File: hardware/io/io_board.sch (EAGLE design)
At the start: 64 parts, among them IC4 74HCT139N, IC5 74AC06N, IC6 8251A, IC7 MAX232, J1 DIN5, T1 BC847, X2 CRYSTALS-NOGND-CFPX-217

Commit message: PCB project fixed
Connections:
- net IO_RD: now also IC3.RD
- net IO_WR: now also IC3.WR
- net RD: no longer IC3.RD
- net WR: no longer IC3.WR

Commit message: Buffer added to D0..D7 lined of CF card
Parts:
- added C26: 100N, rcl:C-EUC0603
- added IC11: 74HCT245DW, 74xx-eu:74HCT245DW
- R5: device rcl:R-EU_R0603 -> rcl:R-EU_0207/10
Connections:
- new net CF_D0: CON1G$1.D00, IC11A.B8
- new net CF_D1: CON1G$1.D01, IC11A.B7
- new net CF_D2: CON1G$1.D02, IC11A.B6
- new net CF_D3: CON1G$1.D03, IC11A.B1
- new net CF_D4: CON1G$1.D04, IC11A.B2
- new net CF_D5: CON1G$1.D05, IC11A.B3
- new net CF_D6: CON1G$1.D06, IC11A.B4
- new net CF_D7: CON1G$1.D07, IC11A.B5
- net CF_CS0: now also IC11A.G
- net D0: now also IC11A.A8; no longer CON1G$1.D00
- net D1: now also IC11A.A7; no longer CON1G$1.D01
- net D2: now also IC11A.A6; no longer CON1G$1.D02
- net D3: now also IC11A.A1; no longer CON1G$1.D03
- net D4: now also IC11A.A2; no longer CON1G$1.D04
- net D5: now also IC11A.A3; no longer CON1G$1.D05
- net D6: now also IC11A.A4; no longer CON1G$1.D06
- net D7: now also IC11A.A5; no longer CON1G$1.D07
- net GND: now also C26.2
- net IO_RD: now also IC11A.DIR
- net VCC: now also C26.1
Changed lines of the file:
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@@
 <?xml version="1.0" encoding="utf-8"?>
 <!DOCTYPE eagle SYSTEM "eagle.dtd">
-<eagle version="7.7.0">
+<eagle version="7.2.0">
 <drawing>
 <settings>
@@
 <part name="R3" library="rcl" deviceset="R-EU_" device="R0603"/>
 <part name="R4" library="rcl" deviceset="R-EU_" device="0204/7"/>
-<part name="R5" library="rcl" deviceset="R-EU_" device="R0603"/>
+<part name="R5" library="rcl" deviceset="R-EU_" device="0207/10"/>
 <part name="R6" library="rcl" deviceset="R-EU_" device="R0603"/>
 <part name="R10" library="rcl" deviceset="R-EU_" device="R0603"/>
@@
 <part name="C25" library="rcl" deviceset="C-EU" device="C0603"/>
 <part name="GND24" library="supply1" deviceset="GND" device=""/>
+<part name="IC11" library="74xx-eu" deviceset="74*245" device="DW" technology="HCT" value="74HCT245DW"/>
+<part name="C26" library="rcl" deviceset="C-EU" device="C0603" value="100N"/>
 </parts>
 <sheets>
@@
 <instance part="C25" gate="G$1" x="180.34" y="236.22" rot="R90"/>
 <instance part="GND24" gate="1" x="190.5" y="236.22" rot="R90"/>
+<instance part="IC11" gate="A" x="7.62" y="-137.16" rot="MR0"/>
+<instance part="C26" gate="G$1" x="-76.2" y="231.14"/>
 </instances>
 <busses>
@@
 <wire x1="-167.64" y1="223.52" x2="-167.64" y2="226.06" width="0.1524" layer="91"/>
 <junction x="-160.02" y="223.52"/>
+<pinref part="C26" gate="G$1" pin="2"/>
+<wire x1="-83.82" y1="223.52" x2="-76.2" y2="223.52" width="0.1524" layer="91"/>
+<wire x1="-76.2" y1="223.52" x2="-76.2" y2="226.06" width="0.1524" layer="91"/>
+<junction x="-83.82" y="223.52"/>
 </segment>
 <segment>
@@
 </segment>
 <segment>
-<pinref part="CON1" gate="G$1" pin="D00"/>
-<wire x1="-55.88" y1="-124.46" x2="-50.8" y2="-124.46" width="0.1524" layer="91"/>
-<label x="-50.8" y="-124.46" size="1.4224" layer="95" xref="yes"/>
+<pinref part="IC11" gate="A" pin="A8"/>
+<wire x1="20.32" y1="-142.24" x2="25.4" y2="-142.24" width="0.1524" layer="91"/>
+<label x="25.4" y="-142.24" size="1.4224" layer="95" xref="yes"/>
 </segment>
 </net>
@@
 </segment>
 <segment>
-<pinref part="CON1" gate="G$1" pin="D01"/>
-<wire x1="-55.88" y1="-127" x2="-50.8" y2="-127" width="0.1524" layer="91"/>
-<label x="-50.8" y="-127" size="1.4224" layer="95" xref="yes"/>
+<pinref part="IC11" gate="A" pin="A7"/>
+<wire x1="20.32" y1="-139.7" x2="25.4" y2="-139.7" width="0.1524" layer="91"/>
+<label x="25.4" y="-139.7" size="1.4224" layer="95" xref="yes"/>
 </segment>
 </net>
@@
 </segment>
 <segment>
-<pinref part="CON1" gate="G$1" pin="D02"/>
-<wire x1="-55.88" y1="-129.54" x2="-50.8" y2="-129.54" width="0.1524" layer="91"/>
-<label x="-50.8" y="-129.54" size="1.4224" layer="95" xref="yes"/>
+<pinref part="IC11" gate="A" pin="A6"/>
+<wire x1="20.32" y1="-137.16" x2="25.4" y2="-137.16" width="0.1524" layer="91"/>
+<label x="25.4" y="-137.16" size="1.4224" layer="95" xref="yes"/>
 </segment>
 </net>
@@
 </segment>
 <segment>
-<pinref part="CON1" gate="G$1" pin="D03"/>
-<wire x1="-55.88" y1="-132.08" x2="-50.8" y2="-132.08" width="0.1524" layer="91"/>
-<label x="-50.8" y="-132.08" size="1.4224" layer="95" xref="yes"/>
+<pinref part="IC11" gate="A" pin="A1"/>
+<wire x1="20.32" y1="-124.46" x2="25.4" y2="-124.46" width="0.1524" layer="91"/>
+<label x="25.4" y="-124.46" size="1.4224" layer="95" xref="yes"/>
 </segment>
 </net>
@@
 </segment>
 <segment>
-<pinref part="CON1" gate="G$1" pin="D04"/>
-<wire x1="-55.88" y1="-134.62" x2="-50.8" y2="-134.62" width="0.1524" layer="91"/>
-<label x="-50.8" y="-134.62" size="1.4224" layer="95" xref="yes"/>
+<pinref part="IC11" gate="A" pin="A2"/>
+<wire x1="20.32" y1="-127" x2="25.4" y2="-127" width="0.1524" layer="91"/>
+<label x="25.4" y="-127" size="1.4224" layer="95" xref="yes"/>
 </segment>
 </net>
@@
 </segment>
 <segment>
-<pinref part="CON1" gate="G$1" pin="D05"/>
-<wire x1="-55.88" y1="-137.16" x2="-50.8" y2="-137.16" width="0.1524" layer="91"/>
-<label x="-50.8" y="-137.16" size="1.4224" layer="95" xref="yes"/>
+<pinref part="IC11" gate="A" pin="A3"/>
+<wire x1="20.32" y1="-129.54" x2="25.4" y2="-129.54" width="0.1524" layer="91"/>
+<label x="25.4" y="-129.54" size="1.4224" layer="95" xref="yes"/>
 </segment>
 </net>
@@
 </segment>
 <segment>
-<pinref part="CON1" gate="G$1" pin="D06"/>
-<wire x1="-55.88" y1="-139.7" x2="-50.8" y2="-139.7" width="0.1524" layer="91"/>
-<label x="-50.8" y="-139.7" size="1.4224" layer="95" xref="yes"/>
+<pinref part="IC11" gate="A" pin="A4"/>
+<wire x1="20.32" y1="-132.08" x2="25.4" y2="-132.08" width="0.1524" layer="91"/>
+<label x="25.4" y="-132.08" size="1.4224" layer="95" xref="yes"/>
 </segment>
 </net>
@@
 </segment>
 <segment>
-<pinref part="CON1" gate="G$1" pin="D07"/>
-<wire x1="-55.88" y1="-142.24" x2="-50.8" y2="-142.24" width="0.1524" layer="91"/>
-<label x="-50.8" y="-142.24" size="1.4224" layer="95" xref="yes"/>
+<pinref part="IC11" gate="A" pin="A5"/>
+<wire x1="20.32" y1="-134.62" x2="25.4" y2="-134.62" width="0.1524" layer="91"/>
+<label x="25.4" y="-134.62" size="1.4224" layer="95" xref="yes"/>
 </segment>
 </net>
@@
 <wire x1="-104.14" y1="63.5" x2="-114.3" y2="63.5" width="0.1524" layer="91"/>
 <label x="-114.3" y="63.5" size="1.4224" layer="95" rot="R180" xref="yes"/>
+</segment>
+<segment>
+<pinref part="IC11" gate="A" pin="DIR"/>
+<wire x1="20.32" y1="-147.32" x2="25.4" y2="-147.32" width="0.1524" layer="91"/>
+<label x="25.4" y="-147.32" size="1.4224" layer="95" xref="yes"/>
 </segment>
 </net>
@@
 <wire x1="-167.64" y1="236.22" x2="-167.64" y2="233.68" width="0.1524" layer="91"/>
 <junction x="-160.02" y="236.22"/>
+<pinref part="C26" gate="G$1" pin="1"/>
+<wire x1="-83.82" y1="236.22" x2="-76.2" y2="236.22" width="0.1524" layer="91"/>
+<wire x1="-76.2" y1="236.22" x2="-76.2" y2="233.68" width="0.1524" layer="91"/>
+<junction x="-83.82" y="236.22"/>
 </segment>
 <segment>
@@
 <label x="71.12" y="-68.58" size="1.4224" layer="95" xref="yes"/>
 </segment>
+<segment>
+<pinref part="IC11" gate="A" pin="G"/>
+<wire x1="20.32" y1="-149.86" x2="25.4" y2="-149.86" width="0.1524" layer="91"/>
+<label x="25.4" y="-149.86" size="1.4224" layer="95" xref="yes"/>
+</segment>
 </net>
 <net name="N$29" class="0">
@@
 </segment>
 </net>
+<net name="CF_D3" class="0">
+<segment>
+<pinref part="CON1" gate="G$1" pin="D03"/>
+<wire x1="-55.88" y1="-132.08" x2="-50.8" y2="-132.08" width="0.1524" layer="91"/>
+<label x="-50.8" y="-132.08" size="1.4224" layer="95" xref="yes"/>
+</segment>
+<segment>
+<pinref part="IC11" gate="A" pin="B1"/>
+<wire x1="-5.08" y1="-124.46" x2="-10.16" y2="-124.46" width="0.1524" layer="91"/>
+<label x="-10.16" y="-124.46" size="1.4224" layer="95" rot="R180" xref="yes"/>
+</segment>
+</net>
+<net name="CF_D4" class="0">
+<segment>
+<pinref part="CON1" gate="G$1" pin="D04"/>
+<wire x1="-55.88" y1="-134.62" x2="-50.8" y2="-134.62" width="0.1524" layer="91"/>
+<label x="-50.8" y="-134.62" size="1.4224" layer="95" xref="yes"/>
+</segment>
+<segment>
+<pinref part="IC11" gate="A" pin="B2"/>
+<wire x1="-5.08" y1="-127" x2="-10.16" y2="-127" width="0.1524" layer="91"/>
+<label x="-10.16" y="-127" size="1.4224" layer="95" rot="R180" xref="yes"/>
+</segment>
+</net>
+<net name="CF_D5" class="0">
+<segment>
+<pinref part="CON1" gate="G$1" pin="D05"/>
+<wire x1="-55.88" y1="-137.16" x2="-50.8" y2="-137.16" width="0.1524" layer="91"/>
+<label x="-50.8" y="-137.16" size="1.4224" layer="95" xref="yes"/>
+</segment>
+<segment>
+<pinref part="IC11" gate="A" pin="B3"/>
+<wire x1="-5.08" y1="-129.54" x2="-10.16" y2="-129.54" width="0.1524" layer="91"/>
+<label x="-10.16" y="-129.54" size="1.4224" layer="95" rot="R180" xref="yes"/>
+</segment>
+</net>
+<net name="CF_D6" class="0">
+<segment>
+<pinref part="CON1" gate="G$1" pin="D06"/>
+<wire x1="-55.88" y1="-139.7" x2="-50.8" y2="-139.7" width="0.1524" layer="91"/>
+<label x="-50.8" y="-139.7" size="1.4224" layer="95" xref="yes"/>
+</segment>
+<segment>
+<pinref part="IC11" gate="A" pin="B4"/>
+<wire x1="-5.08" y1="-132.08" x2="-10.16" y2="-132.08" width="0.1524" layer="91"/>
+<label x="-10.16" y="-132.08" size="1.4224" layer="95" rot="R180" xref="yes"/>
+</segment>
+</net>
+<net name="CF_D7" class="0">
+<segment>
+<pinref part="CON1" gate="G$1" pin="D07"/>
+<wire x1="-55.88" y1="-142.24" x2="-50.8" y2="-142.24" width="0.1524" layer="91"/>
+<label x="-50.8" y="-142.24" size="1.4224" layer="95" xref="yes"/>
+</segment>
+<segment>
+<pinref part="IC11" gate="A" pin="B5"/>
+<wire x1="-5.08" y1="-134.62" x2="-10.16" y2="-134.62" width="0.1524" layer="91"/>
+<label x="-10.16" y="-134.62" size="1.4224" layer="95" rot="R180" xref="yes"/>
+</segment>
+</net>
+<net name="CF_D2" class="0">
+<segment>
+<pinref part="CON1" gate="G$1" pin="D02"/>
+<wire x1="-55.88" y1="-129.54" x2="-50.8" y2="-129.54" width="0.1524" layer="91"/>
+<label x="-50.8" y="-129.54" size="1.4224" layer="95" xref="yes"/>
+</segment>
+<segment>
+<pinref part="IC11" gate="A" pin="B6"/>
+<wire x1="-5.08" y1="-137.16" x2="-10.16" y2="-137.16" width="0.1524" layer="91"/>
+<label x="-10.16" y="-137.16" size="1.4224" layer="95" rot="R180" xref="yes"/>
+</segment>
+</net>
+<net name="CF_D1" class="0">
+<segment>
+<pinref part="CON1" gate="G$1" pin="D01"/>
+<wire x1="-55.88" y1="-127" x2="-50.8" y2="-127" width="0.1524" layer="91"/>
+<label x="-50.8" y="-127" size="1.4224" layer="95" xref="yes"/>
+</segment>
+<segment>
+<pinref part="IC11" gate="A" pin="B7"/>
+<wire x1="-5.08" y1="-139.7" x2="-10.16" y2="-139.7" width="0.1524" layer="91"/>
+<label x="-10.16" y="-139.7" size="1.4224" layer="95" rot="R180" xref="yes"/>
+</segment>
+</net>
+<net name="CF_D0" class="0">
+<segment>
+<pinref part="CON1" gate="G$1" pin="D00"/>
+<wire x1="-55.88" y1="-124.46" x2="-50.8" y2="-124.46" width="0.1524" layer="91"/>
+<label x="-50.8" y="-124.46" size="1.4224" layer="95" xref="yes"/>
+</segment>
+<segment>
+<pinref part="IC11" gate="A" pin="B8"/>
+<wire x1="-5.08" y1="-142.24" x2="-10.16" y2="-142.24" width="0.1524" layer="91"/>
+<label x="-10.16" y="-142.24" size="1.4224" layer="95" rot="R180" xref="yes"/>
+</segment>
+</net>

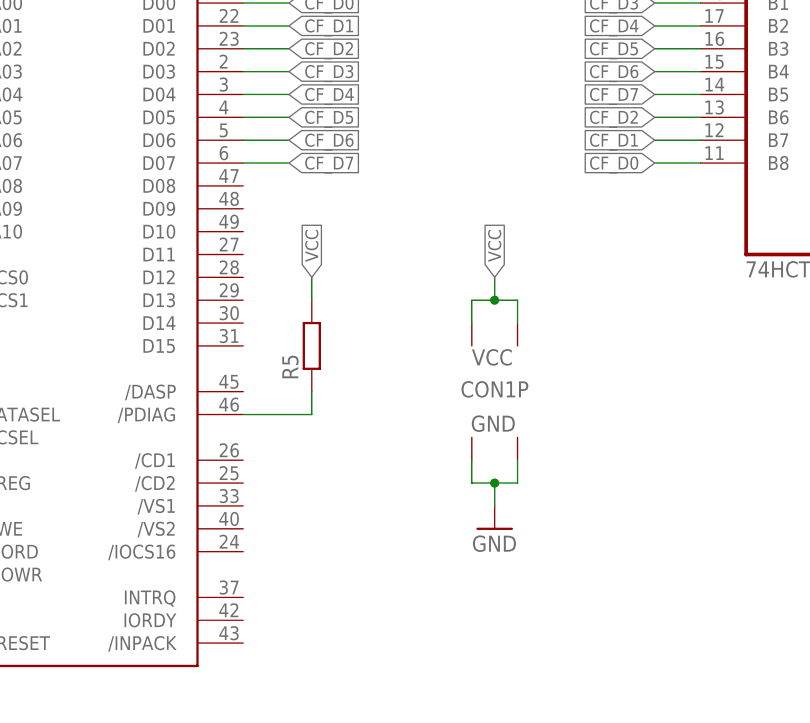
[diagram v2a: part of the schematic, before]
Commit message: CF indidator LED added to IO board
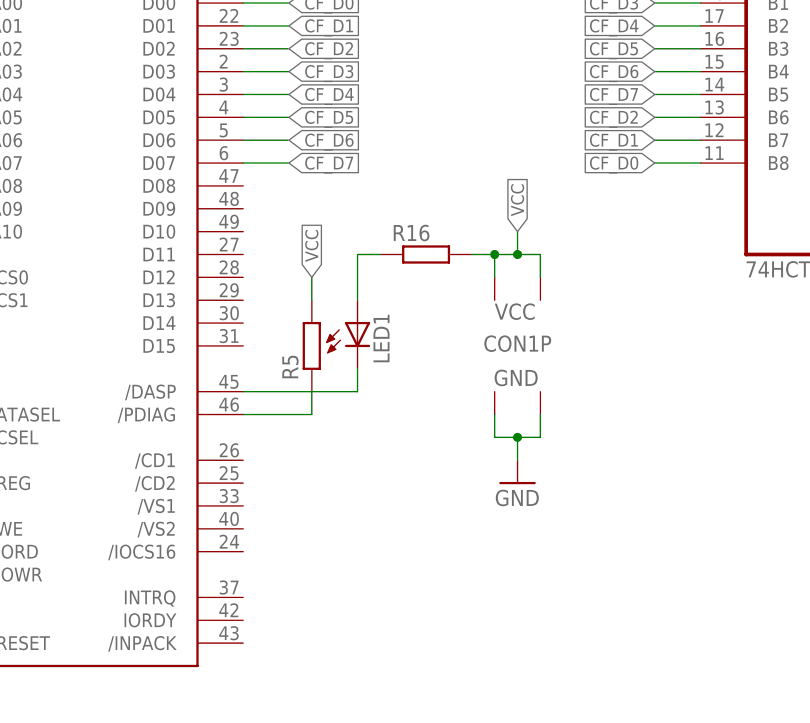
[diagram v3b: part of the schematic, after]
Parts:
- added LED1: (no value), led:LED5MM
- added R16: (no value), rcl:R-EU_R0603
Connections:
- new net N$33: CON1G$1./DASP, LED1.C
- new net N$34: LED1.A, R16.1
- net VCC: now also R16.2
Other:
- moved on the sheet: CON1P
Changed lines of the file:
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@@
 <part name="IC11" library="74xx-eu" deviceset="74*245" device="DW" technology="HCT" value="74HCT245DW"/>
 <part name="C26" library="rcl" deviceset="C-EU" device="C0603" value="100N"/>
+<part name="LED1" library="led" deviceset="LED" device="5MM"/>
+<part name="R16" library="rcl" deviceset="R-EU_" device="R0603"/>
 </parts>
 <sheets>
@@
 <instance part="CON1" gate="G$1" x="-73.66" y="-160.02"/>
 <instance part="GND11" gate="1" x="-93.98" y="-203.2"/>
-<instance part="CON1" gate="P" x="-27.94" y="-167.64"/>
-<instance part="GND13" gate="1" x="-27.94" y="-182.88"/>
+<instance part="CON1" gate="P" x="-25.4" y="-162.56"/>
+<instance part="GND13" gate="1" x="-25.4" y="-177.8"/>
 <instance part="R3" gate="G$1" x="-111.76" y="-165.1" rot="R90"/>
 <instance part="R4" gate="G$1" x="-106.68" y="-165.1" rot="R90"/>
@@
 <instance part="IC11" gate="A" x="7.62" y="-137.16" rot="MR0"/>
 <instance part="C26" gate="G$1" x="-76.2" y="231.14"/>
+<instance part="LED1" gate="G$1" x="-43.18" y="-160.02"/>
+<instance part="R16" gate="G$1" x="-35.56" y="-152.4"/>
 </instances>
 <busses>
@@
 <segment>
 <pinref part="CON1" gate="P" pin="GND1"/>
-<wire x1="-30.48" y1="-175.26" x2="-30.48" y2="-177.8" width="0.1524" layer="91"/>
+<wire x1="-27.94" y1="-170.18" x2="-27.94" y2="-172.72" width="0.1524" layer="91"/>
 <pinref part="CON1" gate="P" pin="GND2"/>
-<wire x1="-30.48" y1="-177.8" x2="-27.94" y2="-177.8" width="0.1524" layer="91"/>
-<wire x1="-27.94" y1="-177.8" x2="-25.4" y2="-177.8" width="0.1524" layer="91"/>
-<wire x1="-25.4" y1="-177.8" x2="-25.4" y2="-175.26" width="0.1524" layer="91"/>
+<wire x1="-27.94" y1="-172.72" x2="-25.4" y2="-172.72" width="0.1524" layer="91"/>
+<wire x1="-25.4" y1="-172.72" x2="-22.86" y2="-172.72" width="0.1524" layer="91"/>
+<wire x1="-22.86" y1="-172.72" x2="-22.86" y2="-170.18" width="0.1524" layer="91"/>
 <pinref part="GND13" gate="1" pin="GND"/>
-<wire x1="-27.94" y1="-180.34" x2="-27.94" y2="-177.8" width="0.1524" layer="91"/>
-<junction x="-27.94" y="-177.8"/>
+<wire x1="-25.4" y1="-175.26" x2="-25.4" y2="-172.72" width="0.1524" layer="91"/>
+<junction x="-25.4" y="-172.72"/>
 </segment>
 <segment>
@@
 <segment>
 <pinref part="CON1" gate="P" pin="VCC1"/>
-<wire x1="-30.48" y1="-160.02" x2="-30.48" y2="-157.48" width="0.1524" layer="91"/>
+<wire x1="-27.94" y1="-154.94" x2="-27.94" y2="-152.4" width="0.1524" layer="91"/>
 <pinref part="CON1" gate="P" pin="VCC2"/>
-<wire x1="-30.48" y1="-157.48" x2="-27.94" y2="-157.48" width="0.1524" layer="91"/>
-<wire x1="-27.94" y1="-157.48" x2="-25.4" y2="-157.48" width="0.1524" layer="91"/>
-<wire x1="-25.4" y1="-157.48" x2="-25.4" y2="-160.02" width="0.1524" layer="91"/>
-<wire x1="-27.94" y1="-157.48" x2="-27.94" y2="-154.94" width="0.1524" layer="91"/>
-<junction x="-27.94" y="-157.48"/>
-<label x="-27.94" y="-154.94" size="1.4224" layer="95" rot="R90" xref="yes"/>
+<wire x1="-27.94" y1="-152.4" x2="-25.4" y2="-152.4" width="0.1524" layer="91"/>
+<wire x1="-25.4" y1="-152.4" x2="-22.86" y2="-152.4" width="0.1524" layer="91"/>
+<wire x1="-22.86" y1="-152.4" x2="-22.86" y2="-154.94" width="0.1524" layer="91"/>
+<wire x1="-25.4" y1="-152.4" x2="-25.4" y2="-149.86" width="0.1524" layer="91"/>
+<junction x="-25.4" y="-152.4"/>
+<label x="-25.4" y="-149.86" size="1.4224" layer="95" rot="R90" xref="yes"/>
+<pinref part="R16" gate="G$1" pin="2"/>
+<wire x1="-27.94" y1="-152.4" x2="-30.48" y2="-152.4" width="0.1524" layer="91"/>
+<junction x="-27.94" y="-152.4"/>
 </segment>
 <segment>
@@
 </segment>
 </net>
+<net name="N$33" class="0">
+<segment>
+<pinref part="CON1" gate="G$1" pin="/DASP"/>
+<pinref part="LED1" gate="G$1" pin="C"/>
+<wire x1="-55.88" y1="-167.64" x2="-43.18" y2="-167.64" width="0.1524" layer="91"/>
+<wire x1="-43.18" y1="-167.64" x2="-43.18" y2="-165.1" width="0.1524" layer="91"/>
+</segment>
+</net>
+<net name="N$34" class="0">
+<segment>
+<pinref part="R16" gate="G$1" pin="1"/>
+<pinref part="LED1" gate="G$1" pin="A"/>
+<wire x1="-40.64" y1="-152.4" x2="-43.18" y2="-152.4" width="0.1524" layer="91"/>
+<wire x1="-43.18" y1="-152.4" x2="-43.18" y2="-157.48" width="0.1524" layer="91"/>
+</segment>
+</net>
